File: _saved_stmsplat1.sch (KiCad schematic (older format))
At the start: 12 parts, among them CN1 C_Pack04-c_pack04, CN10 Conn_01x34_Male, CN7 Conn_01x20_Male, CN8 Conn_01x16_Male, CN9 Conn_01x30_Male, J1 Conn_Coaxial, J2 Conn_Coaxial, J3 Conn_Coaxial, U1 NUCLEO144-F746ZG, U2 SA630D-RF_Switch

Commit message: Getting ready for proper start to project
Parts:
- added U3: MCP6S93-X_UN, spatboard:MCP6S93-X&slash_UN, symbol splatsyms:MCP6S93-X_UN
- CN10: footprint Connector_IDC:IDC-Header_2x17_P2.54mm_Vertical -> spatboard:IDC-Pins_2x17_P2.54mm_Vertical
- CN7: footprint Connector_IDC:IDC-Header_2x10_P2.54mm_Vertical -> spatboard:IDC-Pins_2x10_P2.54mm_Vertical
- CN8: footprint Connector_IDC:IDC-Header_2x08_P2.54mm_Vertical -> spatboard:IDC-Pins_2x8_P2.54mm_Vertical
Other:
- moved on the sheet: CN10, CN7, CN8
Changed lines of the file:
@@
 L Connector:Conn_01x34_Male CN10
 U 1 1 5BD04B56
-P 10150 7350
-F 0 "CN10" H 10256 9128 50  0000 C CNN
-F 1 "Conn_01x34_Male" H 10256 9037 50  0000 C CNN
-F 2 "Connector_IDC:IDC-Header_2x17_P2.54mm_Vertical" H 10150 7350 50  0001 C CNN
-F 3 "~" H 10150 7350 50  0001 C CNN
-	1    10150 7350
+P 9950 6350
+F 0 "CN10" H 10056 8128 50  0000 C CNN
+F 1 "Conn_01x34_Male" H 10056 8037 50  0000 C CNN
+F 2 "spatboard:IDC-Pins_2x17_P2.54mm_Vertical" H 9950 6350 50  0001 C CNN
+F 3 "~" H 9950 6350 50  0001 C CNN
+	1    9950 6350
 	1    0    0    -1
 $EndComp
@@
 L Connector:Conn_01x20_Male CN7
 U 1 1 5BD04C2E
-P 10100 2850
-F 0 "CN7" H 10206 3928 50  0000 C CNN
-F 1 "Conn_01x20_Male" H 10206 3837 50  0000 C CNN
-F 2 "Connector_IDC:IDC-Header_2x10_P2.54mm_Vertical" H 10100 2850 50  0001 C CNN
-F 3 "~" H 10100 2850 50  0001 C CNN
-	1    10100 2850
+P 9450 2900
+F 0 "CN7" H 9556 3978 50  0000 C CNN
+F 1 "Conn_01x20_Male" H 9556 3887 50  0000 C CNN
+F 2 "spatboard:IDC-Pins_2x10_P2.54mm_Vertical" H 9450 2900 50  0001 C CNN
+F 3 "~" H 9450 2900 50  0001 C CNN
+	1    9450 2900
 	1    0    0    -1
 $EndComp
@@
 L Connector:Conn_01x16_Male CN8
 U 1 1 5BD04E48
-P 2650 3350
-F 0 "CN8" H 2756 4228 50  0000 C CNN
-F 1 "Conn_01x16_Male" H 2756 4137 50  0000 C CNN
-F 2 "Connector_IDC:IDC-Header_2x08_P2.54mm_Vertical" H 2650 3350 50  0001 C CNN
-F 3 "~" H 2650 3350 50  0001 C CNN
-	1    2650 3350
+P 2900 3300
+F 0 "CN8" H 3006 4178 50  0000 C CNN
+F 1 "Conn_01x16_Male" H 3006 4087 50  0000 C CNN
+F 2 "spatboard:IDC-Pins_2x8_P2.54mm_Vertical" H 2900 3300 50  0001 C CNN
+F 3 "~" H 2900 3300 50  0001 C CNN
+	1    2900 3300
 	1    0    0    -1
 $EndComp
@@
 	1    0    0    -1
 $EndComp
+$Comp
+L splatsyms:MCP6S93-X_UN U3
+U 1 1 5BD7F0EC
+P 11600 5200
+F 0 "U3" H 12400 5587 60  0000 C CNN
+F 1 "MCP6S93-X_UN" H 12400 5481 60  0000 C CNN
+F 2 "spatboard:MCP6S93-X&slash_UN" H 12400 5440 60  0001 C CNN
+F 3 "" H 11600 5200 60  0000 C CNN
+	1    11600 5200
+	1    0    0    -1
+$EndComp

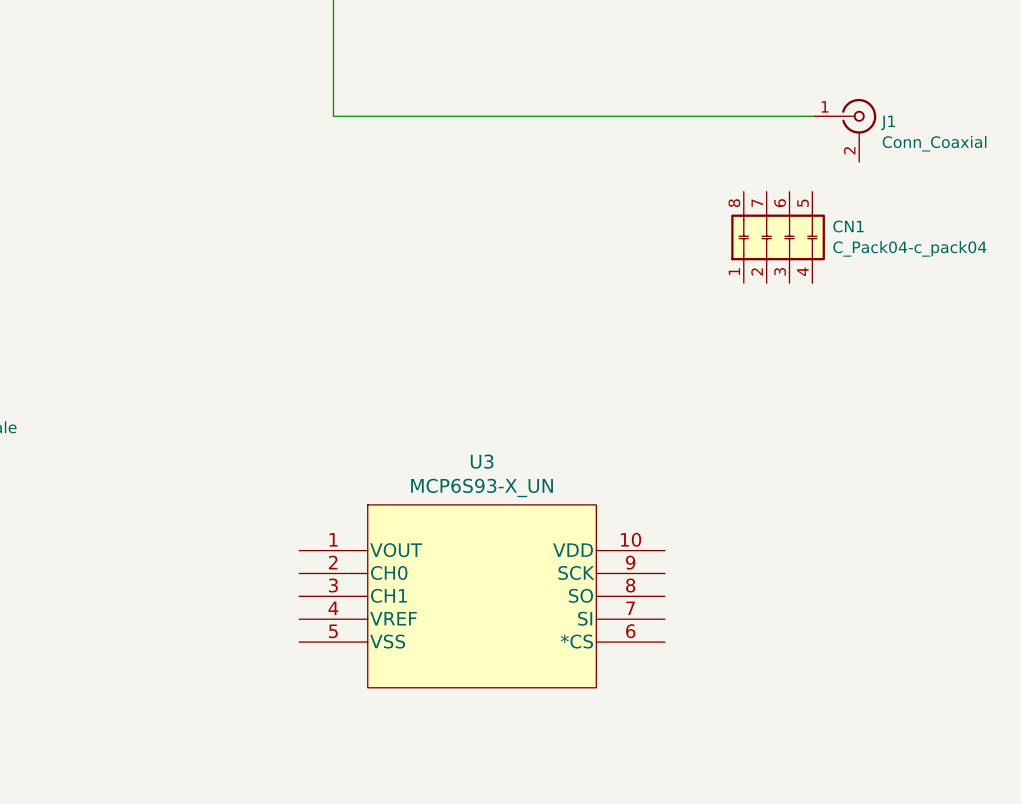
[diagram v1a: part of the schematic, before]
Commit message: Arduino connectors moved to correct position
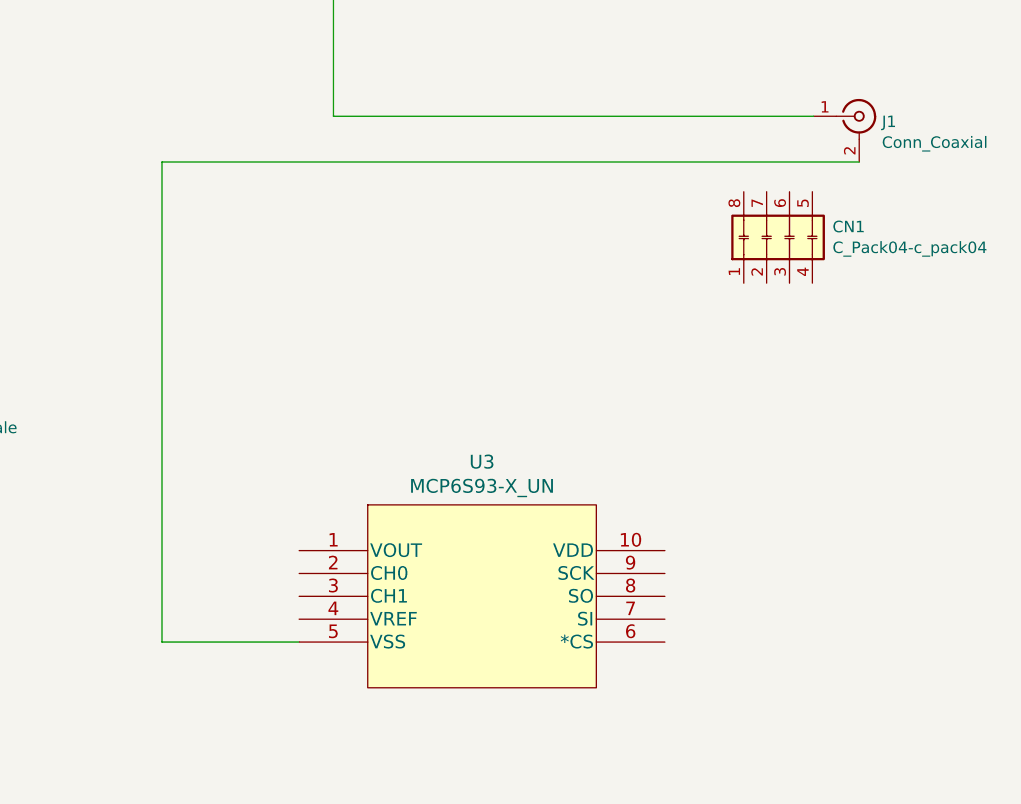
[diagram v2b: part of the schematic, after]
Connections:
- net at J1.2 (Ext): now also U3.5 (VSS)
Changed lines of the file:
@@
 	1    0    0    -1
 $EndComp
+Wire Wire Line
+	14050 3500 11000 3500
+Wire Wire Line
+	11000 3500 11000 5600
+Wire Wire Line
+	11000 5600 11600 5600
 $EndSCHEMATC
